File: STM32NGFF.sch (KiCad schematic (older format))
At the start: 30 parts, among them J1 USB_C_Receptacle_USB2.0, J2 2199119-4, U1 MIC5205-3.3YM5, U2 STM32F303CCTx, U3 USBLC6-2SC6, Y1 16MHz

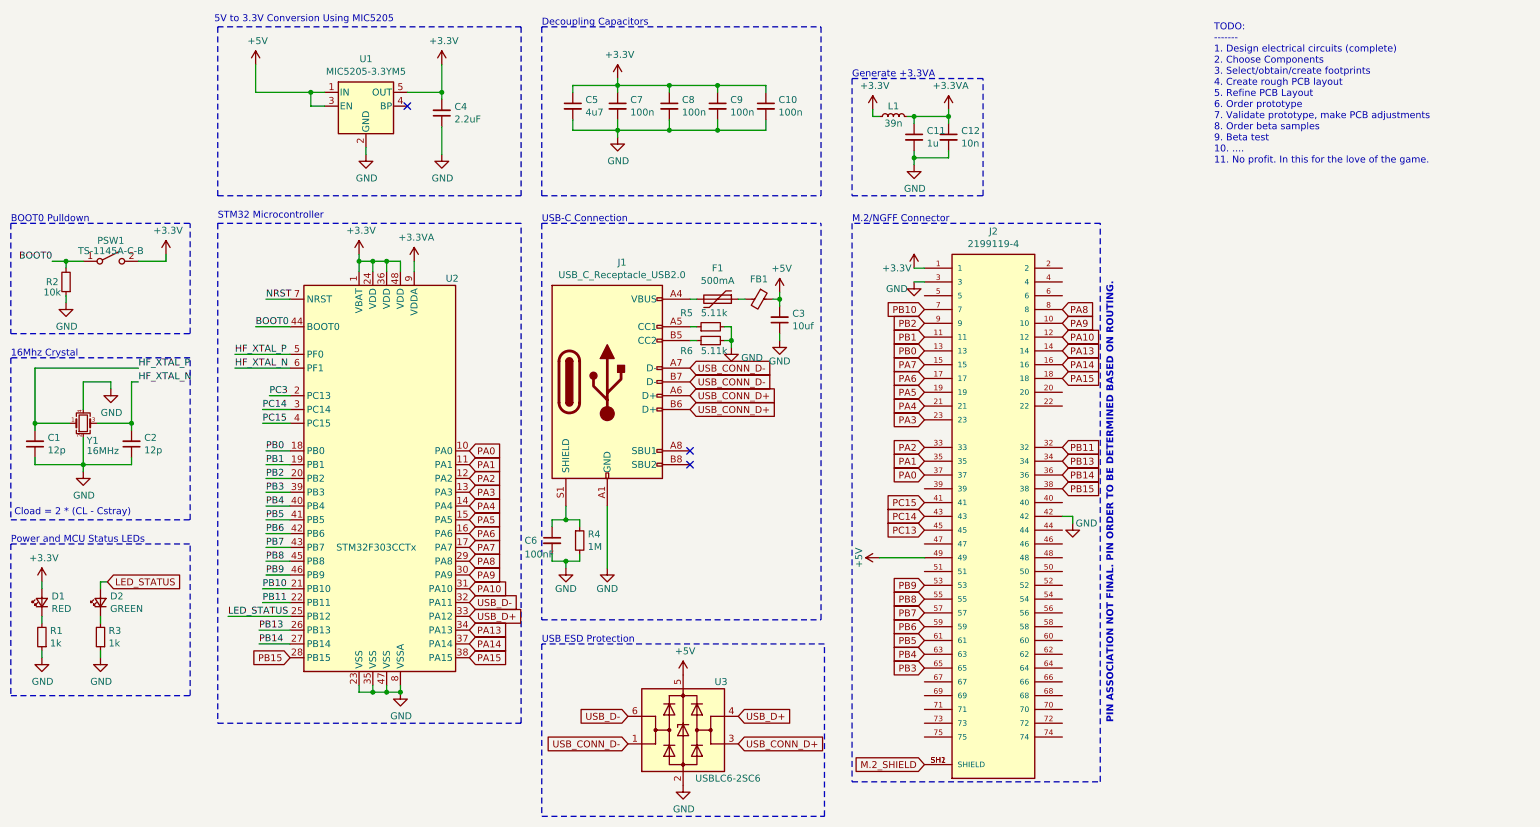
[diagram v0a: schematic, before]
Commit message: Added initial PCB, and updated all global labels to net labels
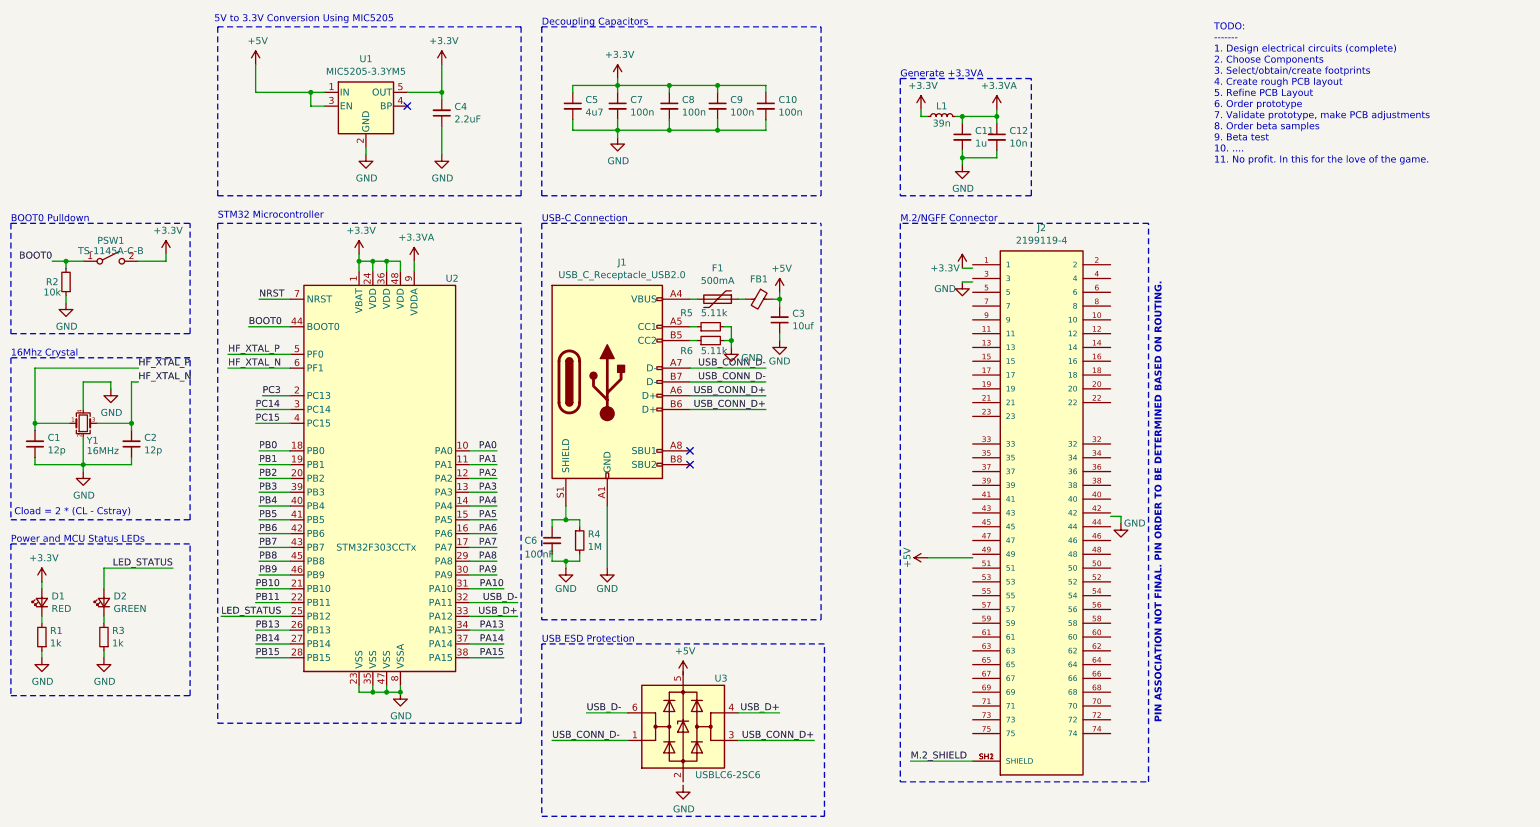
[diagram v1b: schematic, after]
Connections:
- net +3V3: no longer J2.1
- net +5V: no longer J2.49, U3.5 (VBUS)
- net GND: no longer J2.3, J2.42, U3.2 (GND)
- net PA0: no longer J2.37
- net PA1: no longer J2.35
- net PA10: no longer J2.12
- net PA13: no longer J2.14
- net PA14: no longer J2.16
- net PA15: no longer J2.18
- net PA2: no longer J2.33
- net PA3: no longer J2.23
- net PA4: no longer J2.21
- net PA5: no longer J2.19
- net PA6: no longer J2.17
- net PA7: no longer J2.15
- net PA8: no longer J2.8
- net PA9: no longer J2.10
- net PB0: no longer J2.13
- net PB1: no longer J2.11
- net PB10: no longer J2.7
- net PB11: no longer J2.32
- net PB13: no longer J2.34
- net PB14: no longer J2.36
- net PB15: no longer J2.38
- net PB2: no longer J2.9
- net PB3: no longer J2.65
- net PB4: no longer J2.63
- net PB5: no longer J2.61
- net PB6: no longer J2.59
- net PB7: no longer J2.57
- net PB8: no longer J2.55
- net PB9: no longer J2.53
- net PC14: no longer J2.43
- net PC15: no longer J2.41
- net PC13: no longer names the net of J2.45
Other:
- moved on the sheet: C11, C12, D2, J2, L1, R3, U3
